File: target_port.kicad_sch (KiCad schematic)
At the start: 8 parts, among them J3 USB_A, J4 USB_C

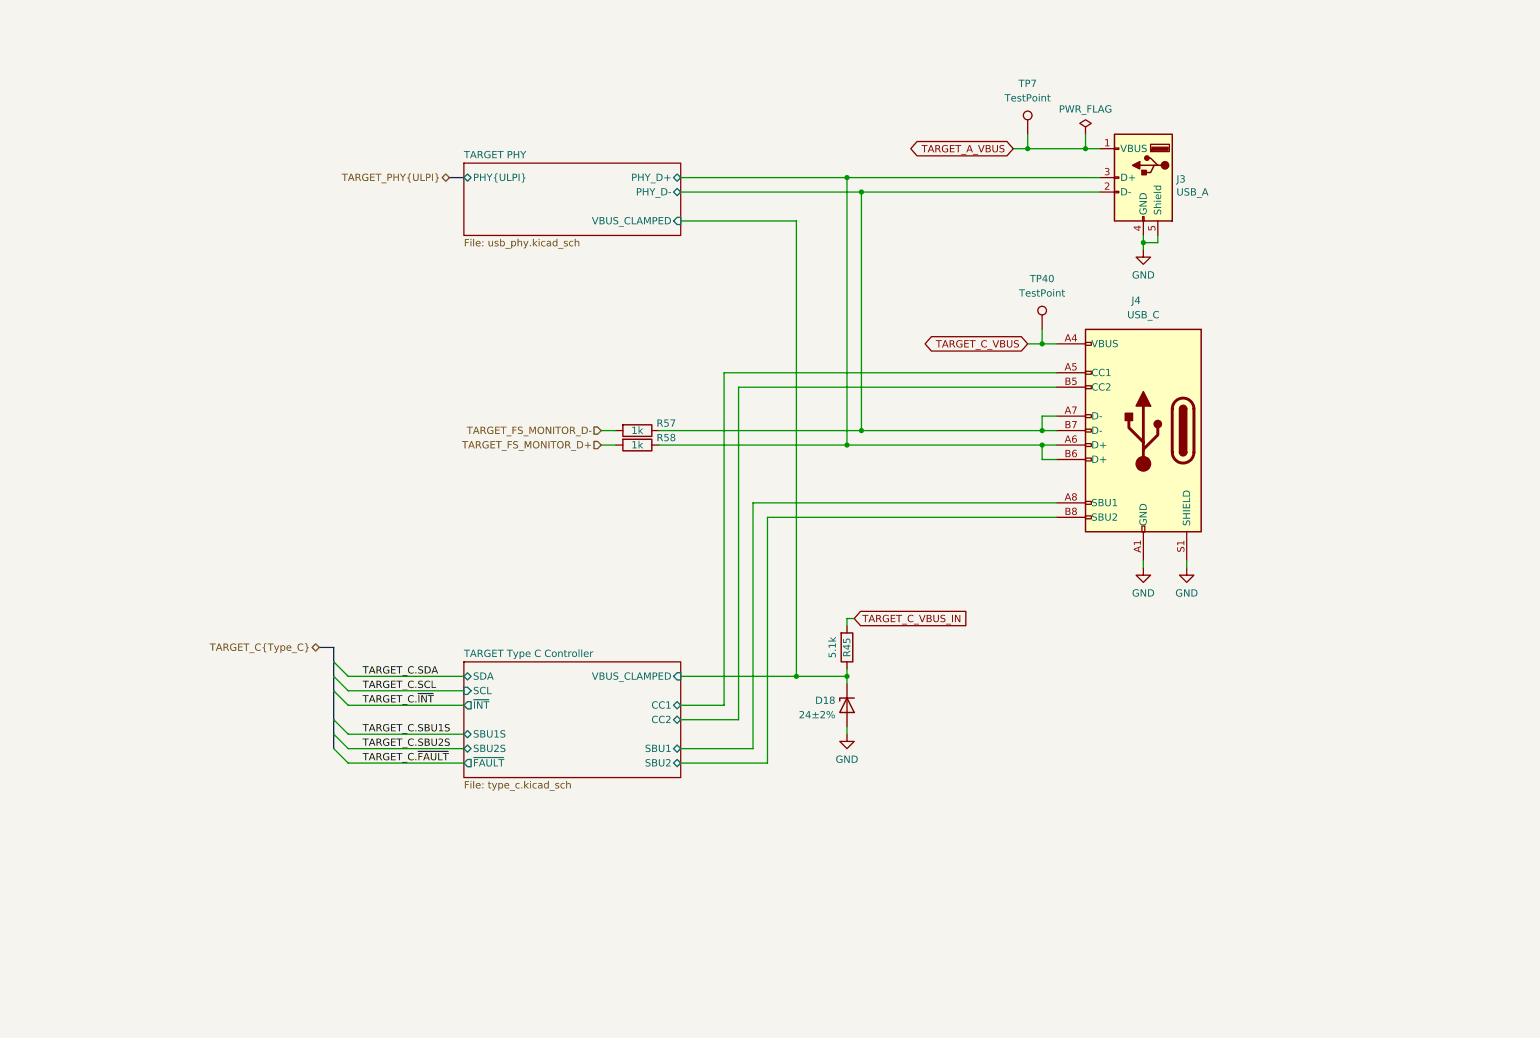
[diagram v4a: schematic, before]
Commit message: Use four-terminal current sense resistor symbol
Previously we had used a special four-terminal symbol and footprint to
ensure that current sense signals did not connect to power supply zones
in multiple places. We rejected this in favor of a two-terminal
schematic symbol and standard resistor footprint to ensure reliable
assembly.

This new solution uses a four-terminal schematic symbol with a
two-terminal footprint which is actually four terminals in two
overlapping pairs using the "net tie" footprint feature.

Fixes #13
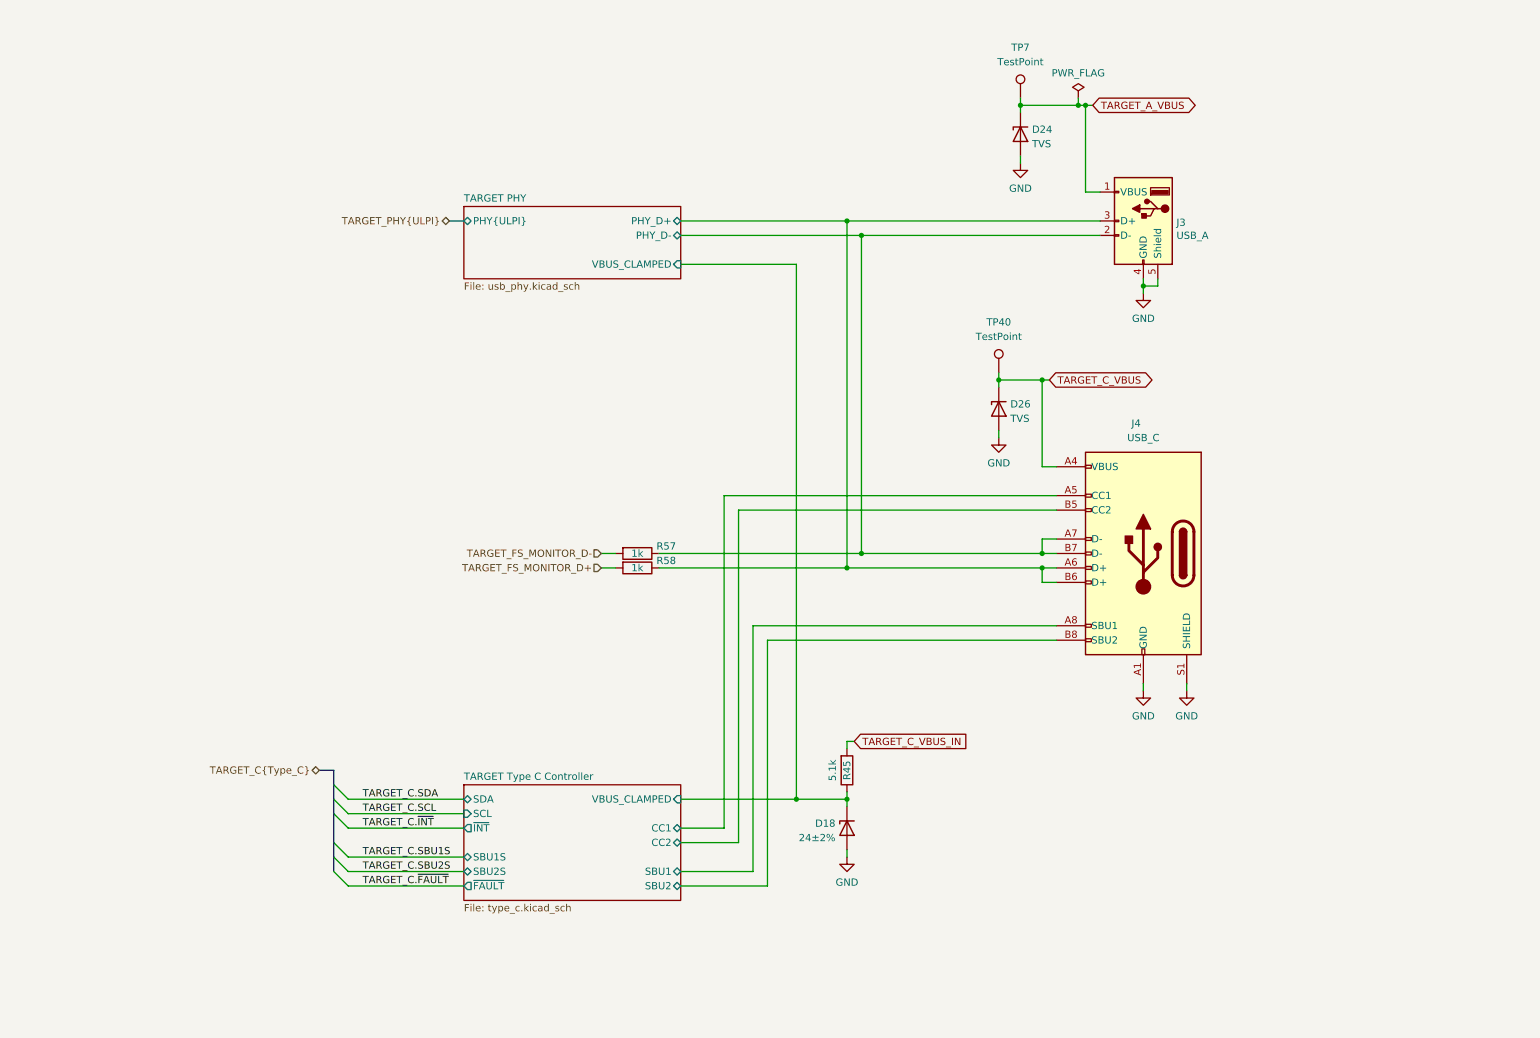
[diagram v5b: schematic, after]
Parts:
- added D24, D26: TVS, cynthion:DFN1006-2, symbol Device:D_Zener
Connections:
- net GND: now also D24.2 (A), D26.2 (A)
- net TARGET_A_VBUS: now also D24.1 (K)
- net TARGET_C_VBUS: now also D26.1 (K)
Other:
- moved on the sheet: D18, J3, J4, R45, R57, R58, TP40, TP7

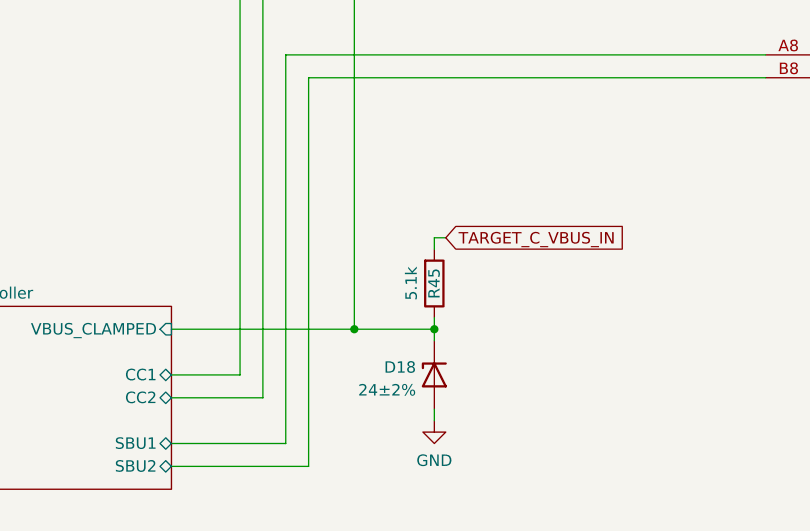
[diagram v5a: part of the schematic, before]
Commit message: Clean up schematic
- Renumber Pmod signal names to match silkscreen labels
- Clean up FPGA symbol
- Clean up PHY symbol
- Add title block to newer sheets
- Fix horizontal line in LED sheet
- Improve various label positions
- Update data sheet fields
- Renumber pages
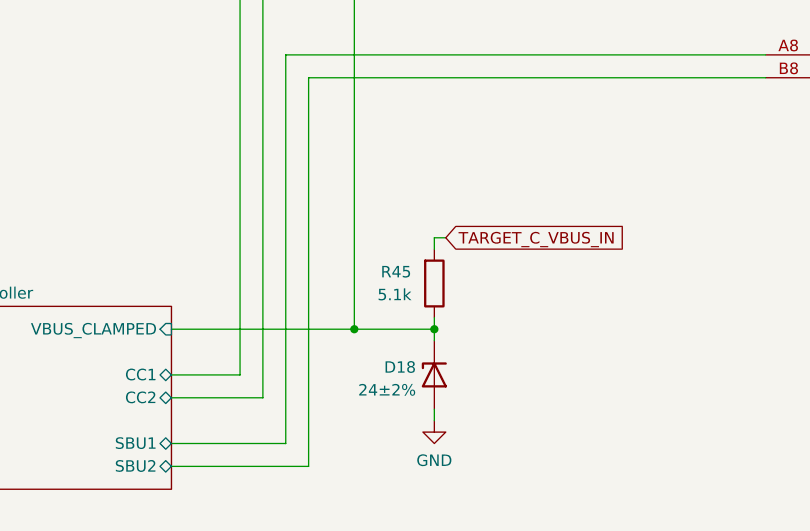
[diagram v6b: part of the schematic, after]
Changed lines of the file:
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@@
   )
   (symbol (lib_id "Device:R") (at 158.75 149.86 0) (mirror x) (unit 1)
-    (in_bom yes) (on_board yes) (dnp no)
-    (property "Reference" "R45" (at 158.75 149.86 90)
-      (effects (font (size 1.27 1.27)))
-    )
-    (property "Value" "5.1k" (at 156.21 149.86 90)
-      (effects (font (size 1.27 1.27)))
+    (in_bom yes) (on_board yes) (dnp no) (fields_autoplaced)
+    (property "Reference" "R45" (at 156.21 148.59 0)
+      (effects (font (size 1.27 1.27)) (justify right))
+    )
+    (property "Value" "5.1k" (at 156.21 151.13 0)
+      (effects (font (size 1.27 1.27)) (justify right))
     )
     (property "Footprint" "Resistor_SMD:R_0402_1005Metric" (at 156.972 149.86 90)
@@
       (effects (font (size 1.27 1.27)) hide)
     )
-    (property "Datasheet" " ~" (at 207.01 54.61 0)
+    (property "Datasheet" "~" (at 207.01 54.61 0)
       (effects (font (size 1.27 1.27)) hide)
     )
@@
     (instances
       (project "cynthion"
-        (path "/fb621148-8145-4217-9712-738e1b5a4823/00000000-0000-0000-0000-00005dddb747" (page "13"))
+        (path "/fb621148-8145-4217-9712-738e1b5a4823/00000000-0000-0000-0000-00005dddb747" (page "8"))
       )
     )
@@
     (instances
       (project "cynthion"
-        (path "/fb621148-8145-4217-9712-738e1b5a4823/00000000-0000-0000-0000-00005dddb747" (page "14"))
-      )
-    )
+        (path "/fb621148-8145-4217-9712-738e1b5a4823/00000000-0000-0000-0000-00005dddb747" (page "9"))
+      )
+    )

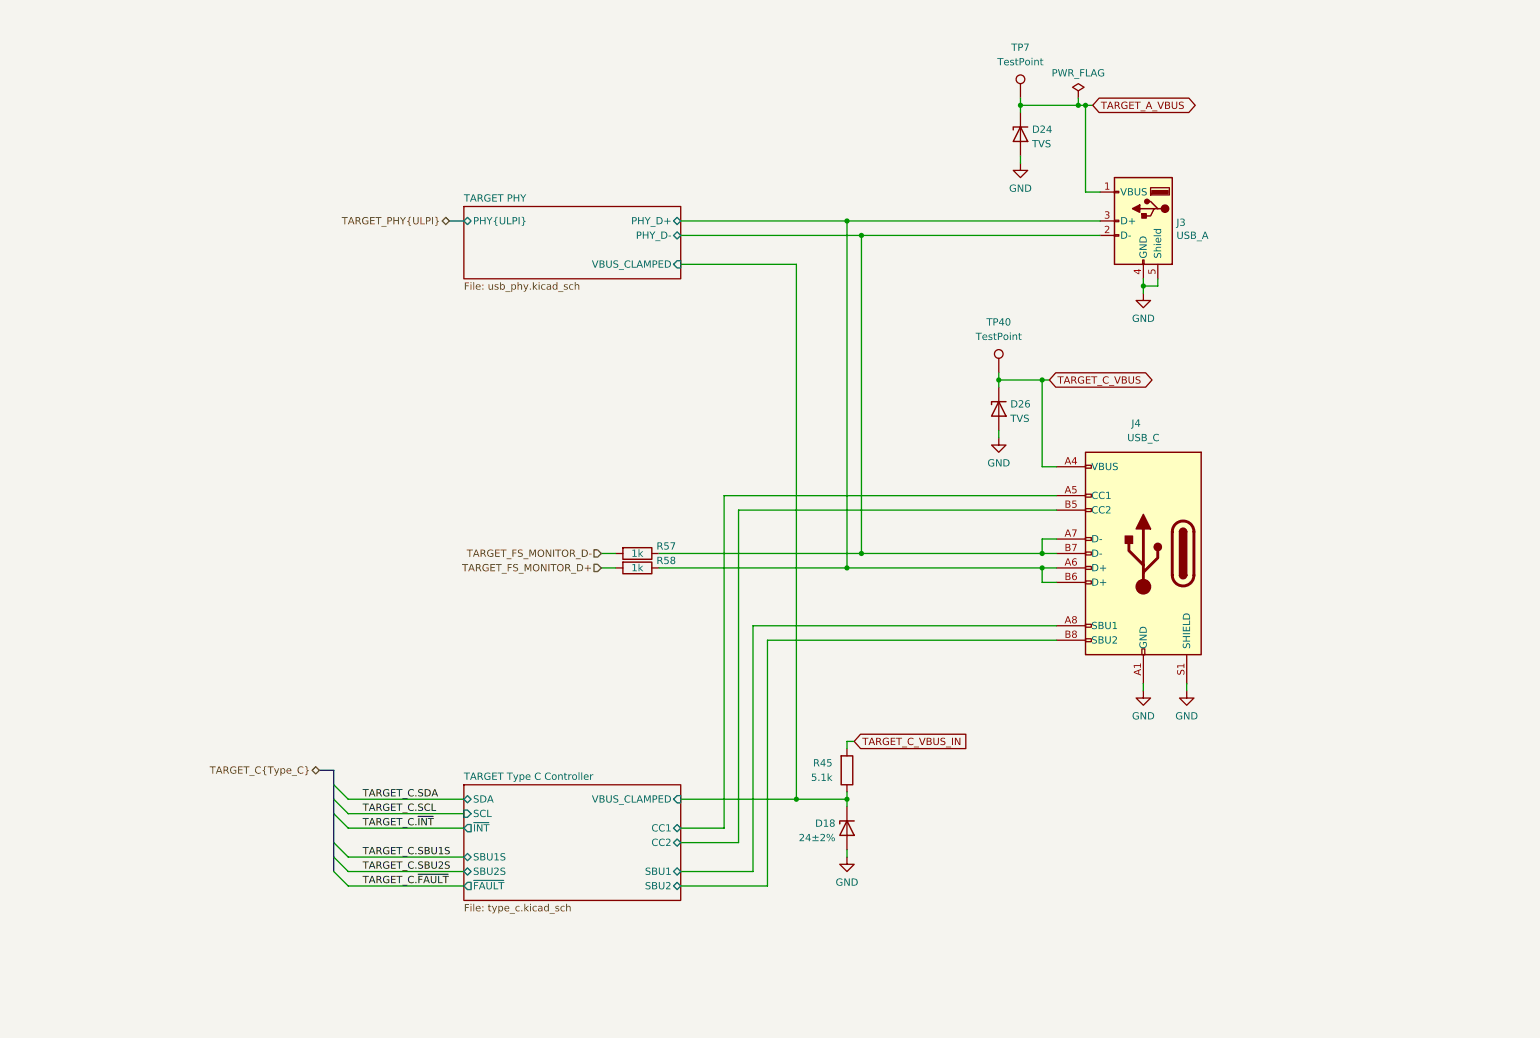
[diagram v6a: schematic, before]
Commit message: Add second common-mode choke for TARGET port
Instead of having a single choke connected in series with the PHY, we
now have a choke in series with each connector. The PHY is connected
between the two chokes.
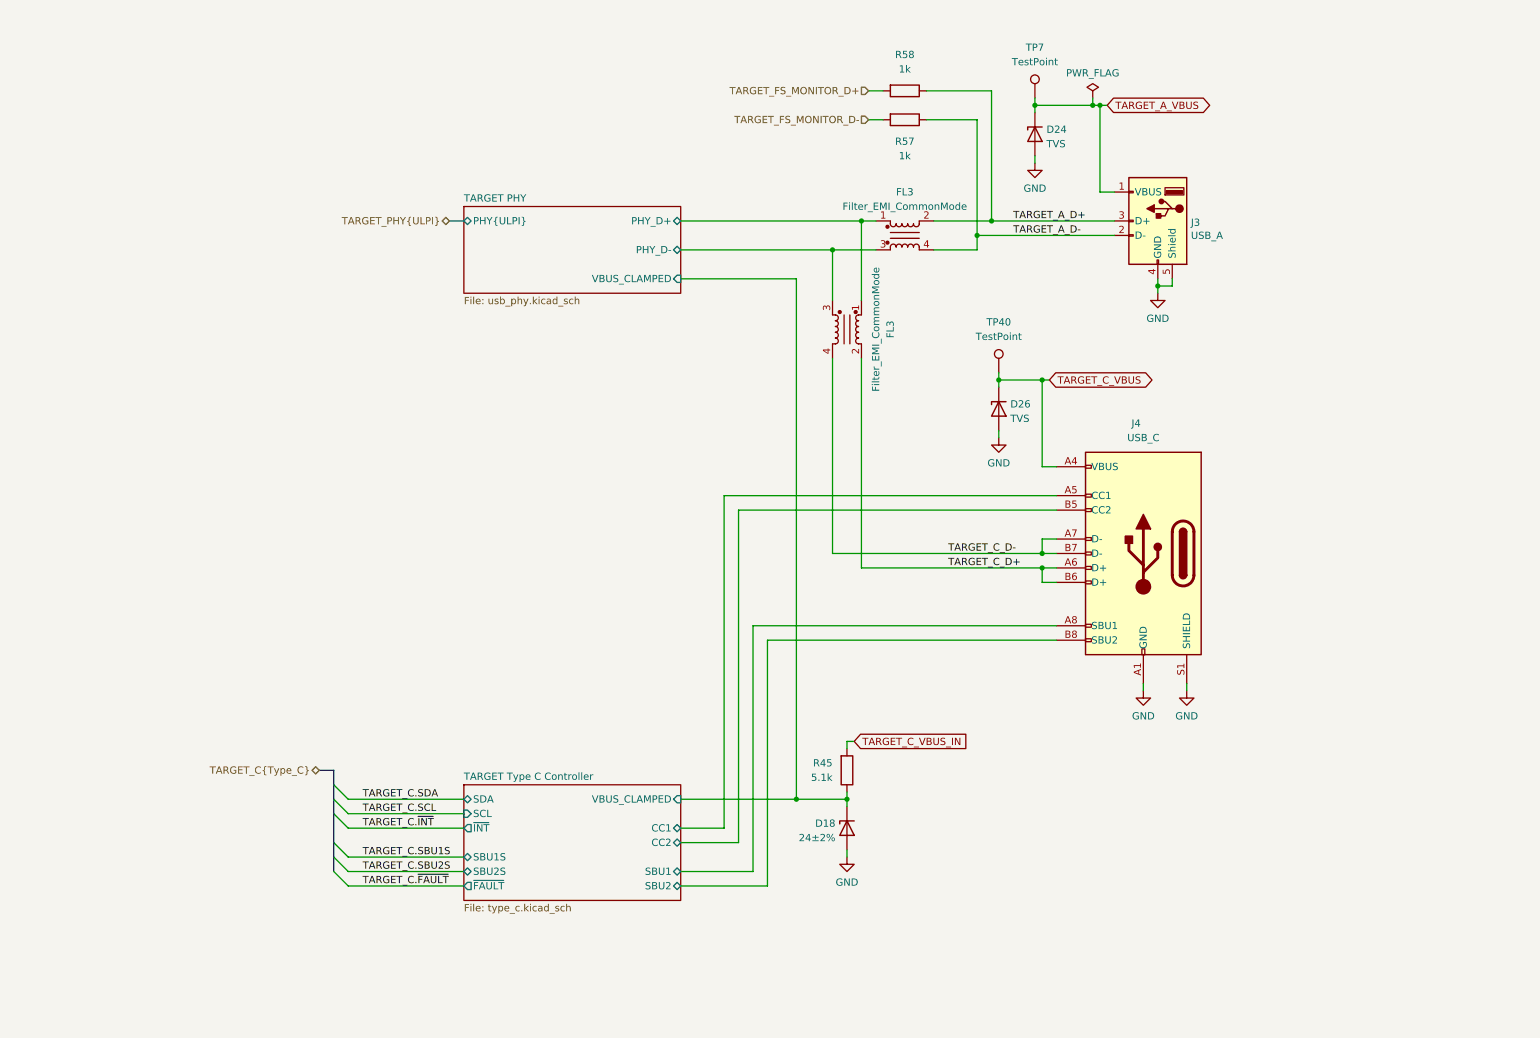
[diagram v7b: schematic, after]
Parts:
- added FL3 (x2): Filter_EMI_CommonMode, cynthion:L_CommonModeChoke_Murata_DLM0NS, symbol Device:Filter_EMI_CommonMode
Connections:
- net TARGET PHY/PHY_D+: now also FL3.1, FL3.1; no longer J3.3 (D+), J4.A6 (D+), J4.B6 (D+), R58.1
- net TARGET PHY/PHY_D-: now also FL3.3, FL3.3; no longer J3.2 (D-), J4.A7 (D-), J4.B7 (D-), R57.1
- new net TARGET_A_D+: FL3.2, J3.3 (D+), R58.1
- new net TARGET_A_D-: FL3.4, J3.2 (D-), R57.1
- new net TARGET_C_D+: FL3.2, J4.A6 (D+), J4.B6 (D+)
- new net TARGET_C_D-: FL3.4, J4.A7 (D-), J4.B7 (D-)
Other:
- moved on the sheet: D24, J3, R57, R58, TP7

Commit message: opened and saved in KiCad 7.0.10
after upgrading from 7.0.9
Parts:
- renumbered FL3 to FL2, FL3 to FL4
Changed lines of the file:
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@@
     (instances
       (project "cynthion"
-        (path "/fb621148-8145-4217-9712-738e1b5a4823/490fda6e-4eae-4b35-a875-405b51914829"
-          (reference "D26") (unit 1)
-        )
         (path "/fb621148-8145-4217-9712-738e1b5a4823/00000000-0000-0000-0000-00005dddb747"
           (reference "D26") (unit 1)
@@
     (instances
       (project "cynthion"
-        (path "/fb621148-8145-4217-9712-738e1b5a4823/490fda6e-4eae-4b35-a875-405b51914829"
+        (path "/fb621148-8145-4217-9712-738e1b5a4823/00000000-0000-0000-0000-00005dddb747"
           (reference "#PWR081") (unit 1)
         )
-        (path "/fb621148-8145-4217-9712-738e1b5a4823/00000000-0000-0000-0000-00005dddb747"
-          (reference "#PWR081") (unit 1)
-        )
       )
     )
@@
     (instances
       (project "cynthion"
-        (path "/fb621148-8145-4217-9712-738e1b5a4823/490fda6e-4eae-4b35-a875-405b51914829"
-          (reference "#PWR039") (unit 1)
-        )
         (path "/fb621148-8145-4217-9712-738e1b5a4823/00000000-0000-0000-0000-00005dddb747"
           (reference "#PWR039") (unit 1)
@@
   (symbol (lib_id "Device:Filter_EMI_CommonMode") (at 168.91 55.88 0) (unit 1)
     (in_bom yes) (on_board yes) (dnp no)
-    (property "Reference" "FL3" (at 168.91 48.26 0)
+    (property "Reference" "FL2" (at 168.91 48.26 0)
       (effects (font (size 1.27 1.27)))
     )
@@
     (instances
       (project "cynthion"
-        (path "/fb621148-8145-4217-9712-738e1b5a4823/00000000-0000-0000-0000-00005dcd9772/86be2f0e-7bb1-42d8-87bc-4230c6dbd013"
-          (reference "FL3") (unit 1)
-        )
-        (path "/fb621148-8145-4217-9712-738e1b5a4823/00000000-0000-0000-0000-00005dd754d4/6ef06f1e-62a2-438c-8ab4-363586d03e74"
-          (reference "FL1") (unit 1)
-        )
-        (path "/fb621148-8145-4217-9712-738e1b5a4823/00000000-0000-0000-0000-00005dddb747/6fe66c21-f87e-45b5-9c98-390633af1111"
-          (reference "FL2") (unit 1)
-        )
         (path "/fb621148-8145-4217-9712-738e1b5a4823/00000000-0000-0000-0000-00005dddb747"
           (reference "FL2") (unit 1)
@@
     (instances
       (project "cynthion"
-        (path "/fb621148-8145-4217-9712-738e1b5a4823/490fda6e-4eae-4b35-a875-405b51914829"
-          (reference "D24") (unit 1)
-        )
         (path "/fb621148-8145-4217-9712-738e1b5a4823/00000000-0000-0000-0000-00005dddb747"
           (reference "D24") (unit 1)
@@
   (symbol (lib_id "Device:Filter_EMI_CommonMode") (at 158.75 72.39 270) (unit 1)
     (in_bom yes) (on_board yes) (dnp no)
-    (property "Reference" "FL3" (at 166.37 72.39 0)
+    (property "Reference" "FL4" (at 166.37 72.39 0)
       (effects (font (size 1.27 1.27)))
     )
@@
     (instances
       (project "cynthion"
-        (path "/fb621148-8145-4217-9712-738e1b5a4823/00000000-0000-0000-0000-00005dcd9772/86be2f0e-7bb1-42d8-87bc-4230c6dbd013"
-          (reference "FL3") (unit 1)
-        )
-        (path "/fb621148-8145-4217-9712-738e1b5a4823/00000000-0000-0000-0000-00005dd754d4/6ef06f1e-62a2-438c-8ab4-363586d03e74"
-          (reference "FL1") (unit 1)
-        )
-        (path "/fb621148-8145-4217-9712-738e1b5a4823/00000000-0000-0000-0000-00005dddb747/6fe66c21-f87e-45b5-9c98-390633af1111"
-          (reference "FL2") (unit 1)
-        )
         (path "/fb621148-8145-4217-9712-738e1b5a4823/00000000-0000-0000-0000-00005dddb747"
           (reference "FL4") (unit 1)
